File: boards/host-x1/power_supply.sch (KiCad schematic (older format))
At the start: 89 parts, among them J1 CONN_3_PWROUT, P1 TESTPOINT, P2 TESTCLIP, P3 TESTCLIP, P4 TESTPOINT, P5 TESTPOINT, U1 OLK-T_3-W12P-C, U2 XC7A100T-1FTG256C, U3 LTC3374-QFN

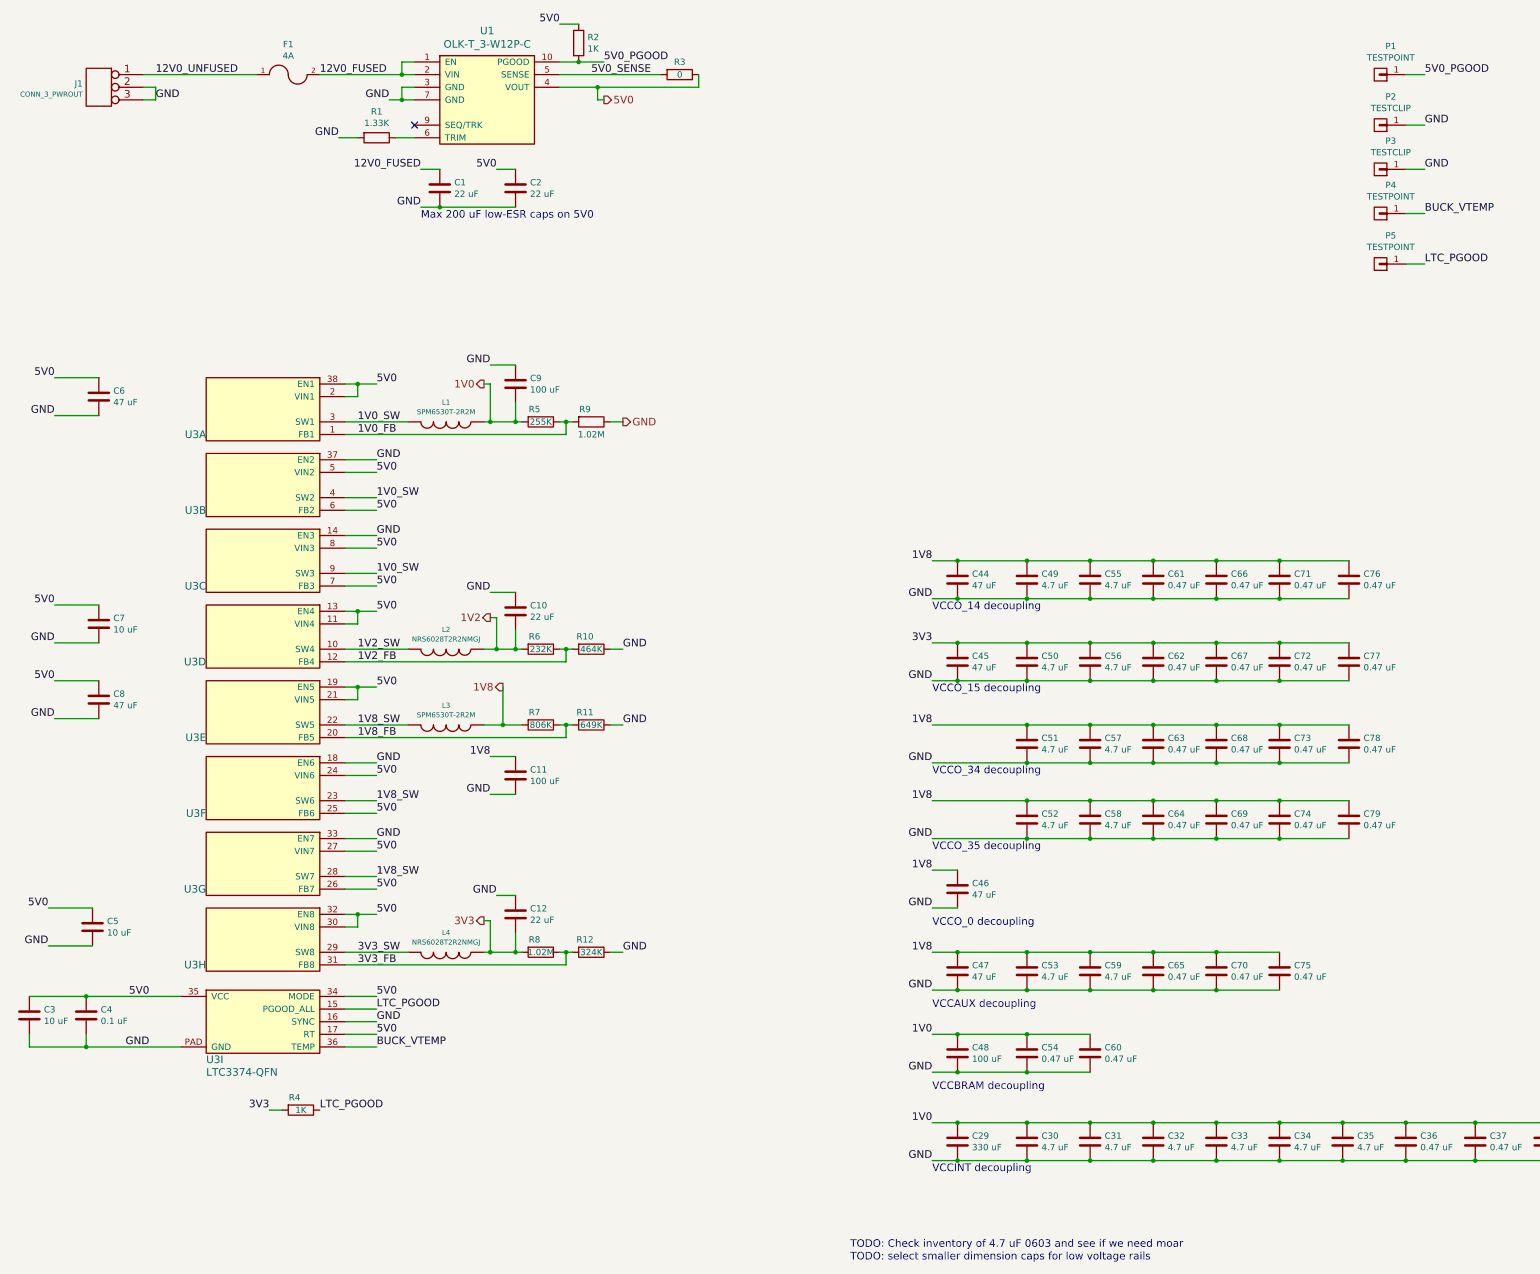
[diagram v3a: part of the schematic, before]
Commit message: Added more test points, various tweaks for debuggability. Clarified values for design review
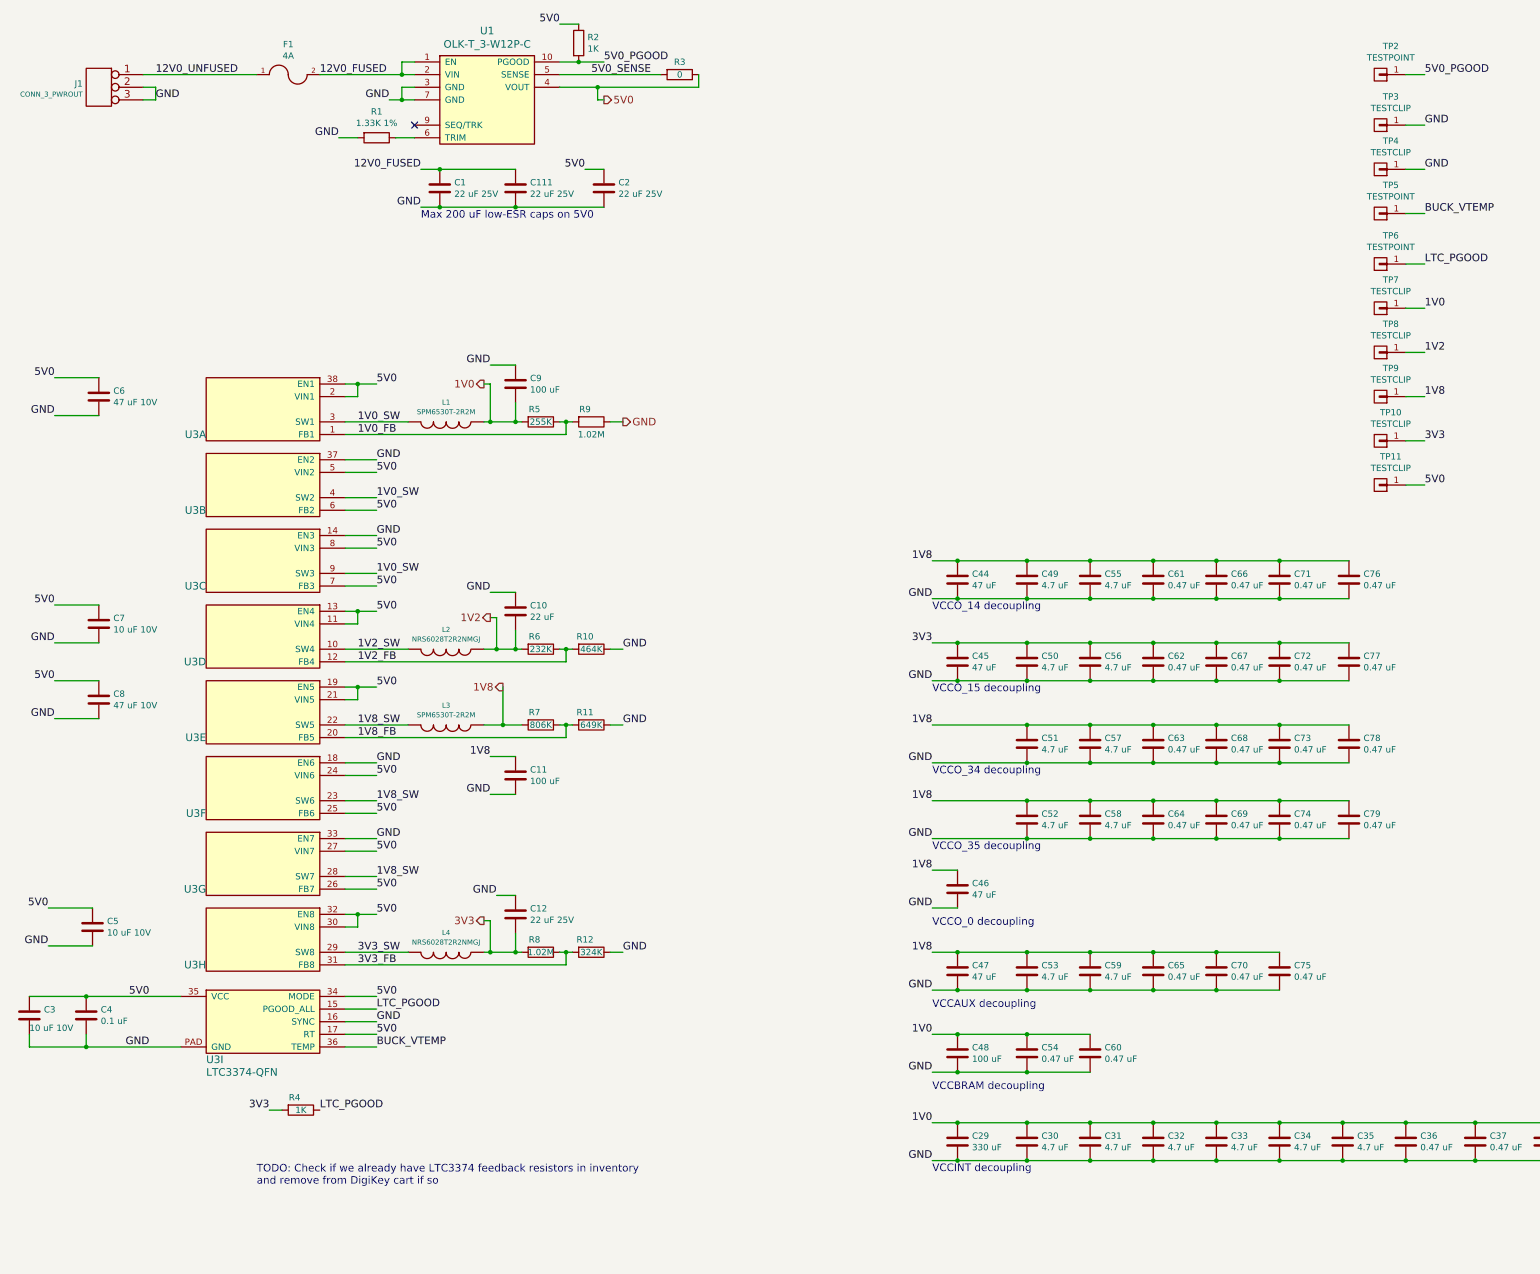
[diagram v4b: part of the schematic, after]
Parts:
- added C111: 22 uF 25V, symbol C
- added TP10, TP11, TP7, TP8, TP9: TESTCLIP, symbol CONN_01X01
- C1, C12, C2: value 22 uF -> 22 uF 25V
- C3, C5, C7: value 10 uF -> 10 uF 10V
- C6, C8: value 47 uF -> 47 uF 10V
- R1: value 1.33K -> 1.33K 1%
- renumbered P1 to TP2, P2 to TP3, P3 to TP4, P4 to TP5, P5 to TP6
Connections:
- net 12V0_FUSED: now also C111.1
- net 1V0: now also TP7.1 (P1)
- net 1V2: now also TP8.1 (P1)
- net 1V8: now also TP9.1 (P1)
- net 3V3: now also TP10.1 (P1)
- net 5V0: now also TP11.1 (P1)
- net GND: now also C111.2
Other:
- note added: "TODO: Check if we already have LTC3374 feedback resistors in inventory\nand remove from DigiKey cart if so"
- note removed: "TODO: Check inventory of 4.7 uF 0603 and see if we need moar"
- note removed: "TODO: select smaller dimension caps for low voltage rails"
- moved on the sheet: C2
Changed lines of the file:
@@
 Sheet 2 6
 Title "STARSHIPRAIDER Single-Lane Host"
-Date "2017-05-06"
+Date "2017-05-07"
 Rev "0.1"
 Comp "Andrew D. Zonenberg"
@@
 P 3400 1500
 F 0 "R1" V 3193 1500 50  0000 C CNN
-F 1 "1.33K" V 3284 1500 50  0000 C CNN
+F 1 "1.33K 1%" V 3284 1500 50  0000 C CNN
 F 2 "" V 3330 1500 50  0000 C CNN
 F 3 "" H 3400 1500 50  0000 C CNN
@@
 P 3900 1900
 F 0 "C1" H 4015 1946 50  0000 L CNN
-F 1 "22 uF" H 4015 1855 50  0000 L CNN
+F 1 "22 uF 25V" H 4015 1855 50  0000 L CNN
 F 2 "" H 3938 1750 50  0000 C CNN
 F 3 "" H 3900 1900 50  0000 C CNN
@@
 L C C2
 U 1 1 590C135A
-P 4500 1900
-F 0 "C2" H 4615 1946 50  0000 L CNN
-F 1 "22 uF" H 4615 1855 50  0000 L CNN
-F 2 "" H 4538 1750 50  0000 C CNN
-F 3 "" H 4500 1900 50  0000 C CNN
-	1    4500 1900
-	1    0    0    -1
-$EndComp
-Text Label 4350 1750 2    60   ~ 0
+P 5200 1900
+F 0 "C2" H 5315 1946 50  0000 L CNN
+F 1 "22 uF 25V" H 5315 1855 50  0000 L CNN
+F 2 "" H 5238 1750 50  0000 C CNN
+F 3 "" H 5200 1900 50  0000 C CNN
+	1    5200 1900
+	1    0    0    -1
+$EndComp
+Text Label 5050 1750 2    60   ~ 0
 5V0
 NoConn ~ 3700 1400
@@
 5V0_PGOOD
 $Comp
-L CONN_01X01 P1
+L CONN_01X01 TP2
 U 1 1 590C1B14
 P 11350 1000
-F 0 "P1" H 11269 775 50  0000 C CNN
+F 0 "TP2" H 11269 775 50  0000 C CNN
 F 1 "TESTPOINT" H 11269 866 50  0000 C CNN
 F 2 "" H 11350 1000 50  0000 C CNN
@@
 5V0_PGOOD
 $Comp
-L CONN_01X01 P2
+L CONN_01X01 TP3
 U 1 1 590C1CD2
 P 11350 1400
-F 0 "P2" H 11269 1175 50  0000 C CNN
+F 0 "TP3" H 11269 1175 50  0000 C CNN
 F 1 "TESTCLIP" H 11269 1266 50  0000 C CNN
 F 2 "" H 11350 1400 50  0000 C CNN
@@
 GND
 $Comp
-L CONN_01X01 P3
+L CONN_01X01 TP4
 U 1 1 590C1DC3
 P 11350 1750
-F 0 "P3" H 11269 1525 50  0000 C CNN
+F 0 "TP4" H 11269 1525 50  0000 C CNN
 F 1 "TESTCLIP" H 11269 1616 50  0000 C CNN
 F 2 "" H 11350 1750 50  0000 C CNN
@@
 BUCK_VTEMP
 $Comp
-L CONN_01X01 P4
+L CONN_01X01 TP5
 U 1 1 590C77F1
 P 11350 2100
-F 0 "P4" H 11269 1875 50  0000 C CNN
+F 0 "TP5" H 11269 1875 50  0000 C CNN
 F 1 "TESTPOINT" H 11269 1966 50  0000 C CNN
 F 2 "" H 11350 2100 50  0000 C CNN
@@
 LTC_PGOOD
 $Comp
-L CONN_01X01 P5
+L CONN_01X01 TP6
 U 1 1 590C7D8D
 P 11350 2500
-F 0 "P5" H 11269 2275 50  0000 C CNN
+F 0 "TP6" H 11269 2275 50  0000 C CNN
 F 1 "TESTPOINT" H 11269 2366 50  0000 C CNN
 F 2 "" H 11350 2500 50  0000 C CNN
@@
 P 1200 3550
 F 0 "C6" H 1315 3596 50  0000 L CNN
-F 1 "47 uF" H 1315 3505 50  0000 L CNN
+F 1 "47 uF 10V" H 1315 3505 50  0000 L CNN
 F 2 "" H 1238 3400 50  0000 C CNN
 F 3 "" H 1200 3550 50  0000 C CNN
@@
 P 1200 5950
 F 0 "C8" H 1315 5996 50  0000 L CNN
-F 1 "47 uF" H 1315 5905 50  0000 L CNN
+F 1 "47 uF 10V" H 1315 5905 50  0000 L CNN
 F 2 "" H 1238 5800 50  0000 C CNN
 F 3 "" H 1200 5950 50  0000 C CNN
@@
 P 1200 5350
 F 0 "C7" H 1315 5396 50  0000 L CNN
-F 1 "10 uF" H 1315 5305 50  0000 L CNN
+F 1 "10 uF 10V" H 1315 5305 50  0000 L CNN
 F 2 "" H 1238 5200 50  0000 C CNN
 F 3 "" H 1200 5350 50  0000 C CNN
@@
 P 1150 7750
 F 0 "C5" H 1265 7796 50  0000 L CNN
-F 1 "10 uF" H 1265 7705 50  0000 L CNN
+F 1 "10 uF 10V" H 1265 7705 50  0000 L CNN
 F 2 "" H 1188 7600 50  0000 C CNN
 F 3 "" H 1150 7750 50  0000 C CNN
@@
 P 4500 7650
 F 0 "C12" H 4615 7696 50  0000 L CNN
-F 1 "22 uF" H 4615 7605 50  0000 L CNN
+F 1 "22 uF 25V" H 4615 7605 50  0000 L CNN
 F 2 "" H 4538 7500 50  0000 C CNN
 F 3 "" H 4500 7650 50  0000 C CNN
@@
 P 650 8450
 F 0 "C3" H 765 8496 50  0000 L CNN
-F 1 "10 uF" H 765 8405 50  0000 L CNN
+F 1 "10 uF 10V" H 650 8350 50  0000 L CNN
 F 2 "" H 688 8300 50  0000 C CNN
 F 3 "" H 650 8450 50  0000 C CNN
@@
 	1    0    0    -1
 $EndComp
-Text Notes 7150 10300 0    60   ~ 0
-TODO: Check inventory of 4.7 uF 0603 and see if we need moar
 $Comp
 L C C31
@@
 Connection ~ 3600 1200
 Wire Wire Line
-	3750 2050 4500 2050
-Wire Wire Line
-	3750 1750 3900 1750
+	3750 2050 5200 2050
+Wire Wire Line
+	3750 1750 4500 1750
 Wire Wire Line
 	4850 1100 5950 1100
 Wire Wire Line
-	4350 1750 4500 1750
+	5050 1750 5200 1750
 Connection ~ 3900 2050
 Wire Wire Line
@@
 Connection ~ 8550 7950
 Connection ~ 8000 7950
-Text Notes 7150 10400 0    60   ~ 0
-TODO: select smaller dimension caps for low voltage rails
 Text Notes 7800 7750 0    60   ~ 0
 VCCO_0 decoupling
@@
 Wire Wire Line
 	2950 1000 3700 1000
+$Comp
+L C C111
+U 1 1 591301E3
+P 4500 1900
+F 0 "C111" H 4615 1946 50  0000 L CNN
+F 1 "22 uF 25V" H 4615 1855 50  0000 L CNN
+F 2 "" H 4538 1750 50  0000 C CNN
+F 3 "" H 4500 1900 50  0000 C CNN
+	1    4500 1900
+	1    0    0    -1
+$EndComp
+Connection ~ 3900 1750
+Connection ~ 4500 2050
+Text Notes 2450 9800 0    60   ~ 0
+TODO: Check if we already have LTC3374 feedback resistors in inventory\nand remove from DigiKey cart if so
+$Comp
+L CONN_01X01 TP7
+U 1 1 59134315
+P 11350 2850
+F 0 "TP7" H 11269 2625 50  0000 C CNN
+F 1 "TESTCLIP" H 11269 2716 50  0000 C CNN
+F 2 "" H 11350 2850 50  0000 C CNN
+F 3 "" H 11350 2850 50  0000 C CNN
+	1    11350 2850
+	-1   0    0    1
+$EndComp
+Text Label 11700 2850 0    60   ~ 0
+1V0
+Wire Wire Line
+	11700 2850 11550 2850
+$Comp
+L CONN_01X01 TP8
+U 1 1 591345F5
+P 11350 3200
+F 0 "TP8" H 11269 2975 50  0000 C CNN
+F 1 "TESTCLIP" H 11269 3066 50  0000 C CNN
+F 2 "" H 11350 3200 50  0000 C CNN
+F 3 "" H 11350 3200 50  0000 C CNN
+	1    11350 3200
+	-1   0    0    1
+$EndComp
+Text Label 11700 3200 0    60   ~ 0
+1V2
+Wire Wire Line
+	11700 3200 11550 3200
+$Comp
+L CONN_01X01 TP9
+U 1 1 591349A0
+P 11350 3550
+F 0 "TP9" H 11269 3325 50  0000 C CNN
+F 1 "TESTCLIP" H 11269 3416 50  0000 C CNN
+F 2 "" H 11350 3550 50  0000 C CNN
+F 3 "" H 11350 3550 50  0000 C CNN
+	1    11350 3550
+	-1   0    0    1
+$EndComp
+Text Label 11700 3550 0    60   ~ 0
+1V8
+Wire Wire Line
+	11700 3550 11550 3550
+$Comp
+L CONN_01X01 TP10
+U 1 1 59134C86
+P 11350 3900
+F 0 "TP10" H 11269 3675 50  0000 C CNN
+F 1 "TESTCLIP" H 11269 3766 50  0000 C CNN
+F 2 "" H 11350 3900 50  0000 C CNN
+F 3 "" H 11350 3900 50  0000 C CNN
+	1    11350 3900
+	-1   0    0    1
+$EndComp
+Text Label 11700 3900 0    60   ~ 0
+3V3
+Wire Wire Line
+	11700 3900 11550 3900
+$Comp
+L CONN_01X01 TP11
+U 1 1 591351D3
+P 11350 4250
+F 0 "TP11" H 11269 4025 50  0000 C CNN
+F 1 "TESTCLIP" H 11269 4116 50  0000 C CNN
+F 2 "" H 11350 4250 50  0000 C CNN
+F 3 "" H 11350 4250 50  0000 C CNN
+	1    11350 4250
+	-1   0    0    1
+$EndComp
+Text Label 11700 4250 0    60   ~ 0
+5V0
+Wire Wire Line
+	11700 4250 11550 4250
 $EndSCHEMATC

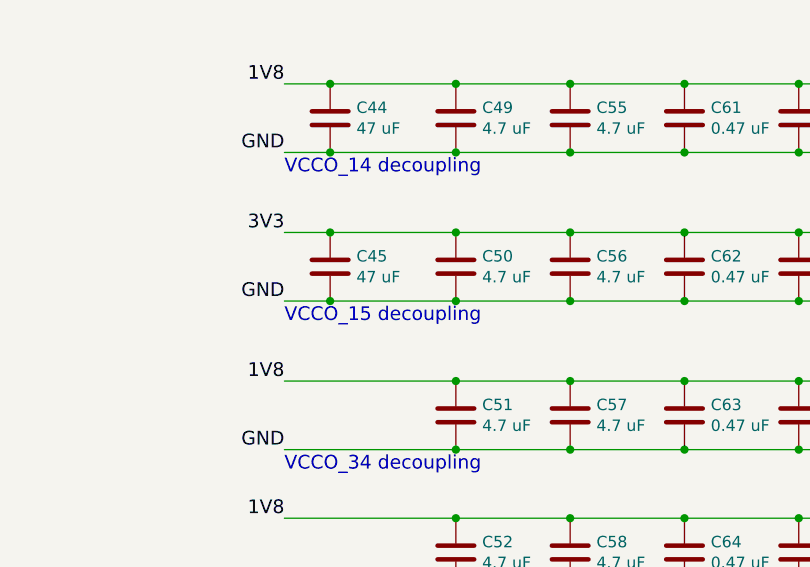
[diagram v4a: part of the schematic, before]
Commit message: Finished initial schematic and component assignments, ready for layout
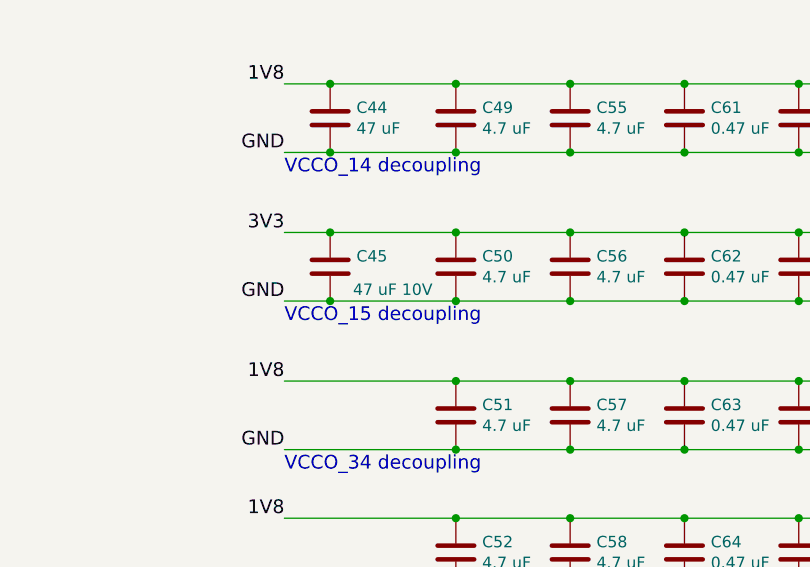
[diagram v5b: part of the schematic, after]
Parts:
- C1, C11, C111, C12, C2, C29, C48, C6, C8, C9: footprint (none) -> azonenberg_pcb:EIA_1210_CAP_NOSILK
- C10, C44, C46, C47: footprint (none) -> azonenberg_pcb:EIA_0805_CAP_NOSILK
- C3, C5, C7: footprint (none) -> azonenberg_pcb:EIA_1206_CAP_NOSILK
- C30, C31, C32, C33, C34, C35, C49, C50, C51, C52, C53, C55, C56, C57, C58, C59: footprint (none) -> azonenberg_pcb:EIA_0603_CAP_NOSILK
- C36, C37, C38, C39, C4, C40, C41, C42, C43, C54, C60, C61, C62, C63, C64, C65, C66, C67, C68, C69, C70, C71, C72, C73, C74, C75, C76, C77, C78, C79: footprint (none) -> azonenberg_pcb:EIA_0402_CAP_NOSILK
- C45: value 47 uF -> 47 uF 10V; footprint (none) -> azonenberg_pcb:EIA_1210_CAP_NOSILK
- F1, R1, R10, R11, R12, R2, R3, R4, R5, R6, R7, R8, R9: footprint (none) -> azonenberg_pcb:EIA_0402_RES_NOSILK
- J1: footprint (none) -> azonenberg_pcb:CONN_CUI_PJ-058BH_HIPWR_BARREL_NOSLOT
- L1, L3: footprint (none) -> azonenberg_pcb:INDUCTOR_TDK_SPM6530
- L2, L4: footprint (none) -> azonenberg_pcb:INDUCTOR_YUDEN_NR6028
- TP10, TP11, TP3, TP4, TP7, TP8, TP9: footprint (none) -> azonenberg_pcb:TESTPOINT_SMT_KEYSTONE_5016
- TP2, TP5, TP6: footprint (none) -> azonenberg_pcb:TESTPOINT_SMT_0.5MM
- U1: footprint (none) -> azonenberg_pcb:MODULE_MURATA_OKL-T3-W12
- U2: footprint (none) -> azonenberg_pcb:BGA_256_17x17_FULLARRAY_1MM
- U3: footprint (none) -> azonenberg_pcb:QFN_38_0.5MM_5x7MM

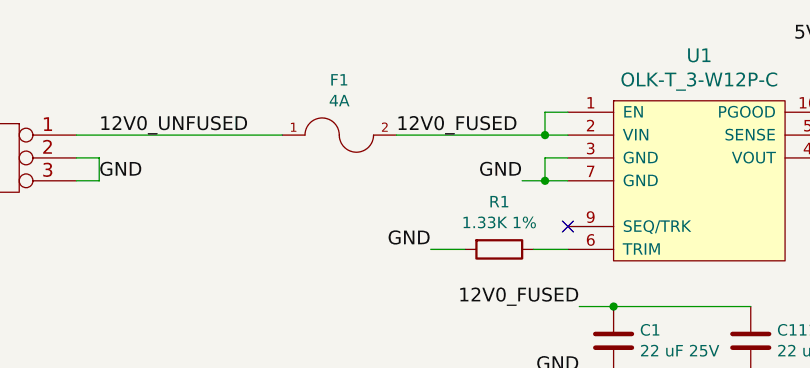
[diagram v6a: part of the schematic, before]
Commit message: Added 12V0 to expansion card connector
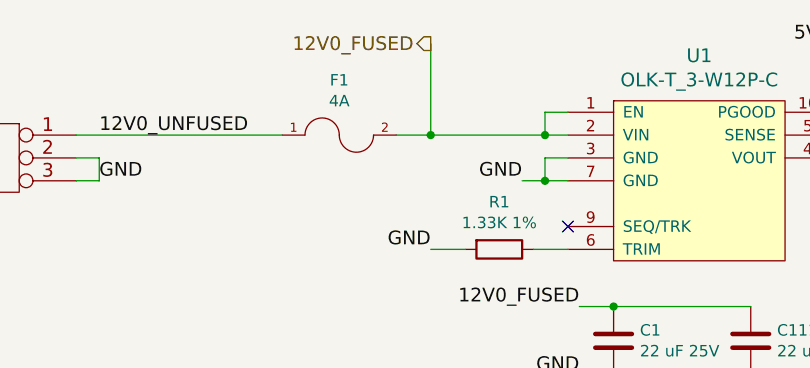
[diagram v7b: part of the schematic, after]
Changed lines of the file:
@@
 Text Label 1650 1200 0    60   ~ 0
 GND
-Text Label 2950 1000 0    60   ~ 0
-12V0_FUSED
 $Comp
 L XC7AxT-xFTG256x U?
@@
 Wire Wire Line
 	11700 4250 11550 4250
+Text HLabel 3100 600  0    60   Output ~ 0
+12V0_FUSED
+Wire Wire Line
+	3100 600  3100 1000
+Connection ~ 3100 1000
 $EndSCHEMATC
